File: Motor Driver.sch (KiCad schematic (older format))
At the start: 45 parts, among them CON1 AVR-ISP-6, J1 Conn_01x02, J10 Conn_01x04, J2 Conn_01x02, J3 Conn_01x04, J4 Conn_01x04, J5 Conn_01x04, J6 Conn_02x02_Odd_Even, J7 Conn_01x02, J8 Conn_01x02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

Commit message: Added Isolation
Added an Optoisolator to isolate the input signal
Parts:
- added J11: Conn_01x02, Pin_Headers:Pin_Header_Straight_1x02_Pitch2.54mm, symbol Conn_01x02
- added R14, R15, R16: 200, Resistors_THT:R_Axial_DIN0207_L6.3mm_D2.5mm_P7.62mm_Horizontal, symbol R
- added U2: PC817, Housings_DIP:DIP-4_W7.62mm, symbol PC817
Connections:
- net labels added: INPUT_L
- wire segments 141 -> 152
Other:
- moved on the sheet: J1

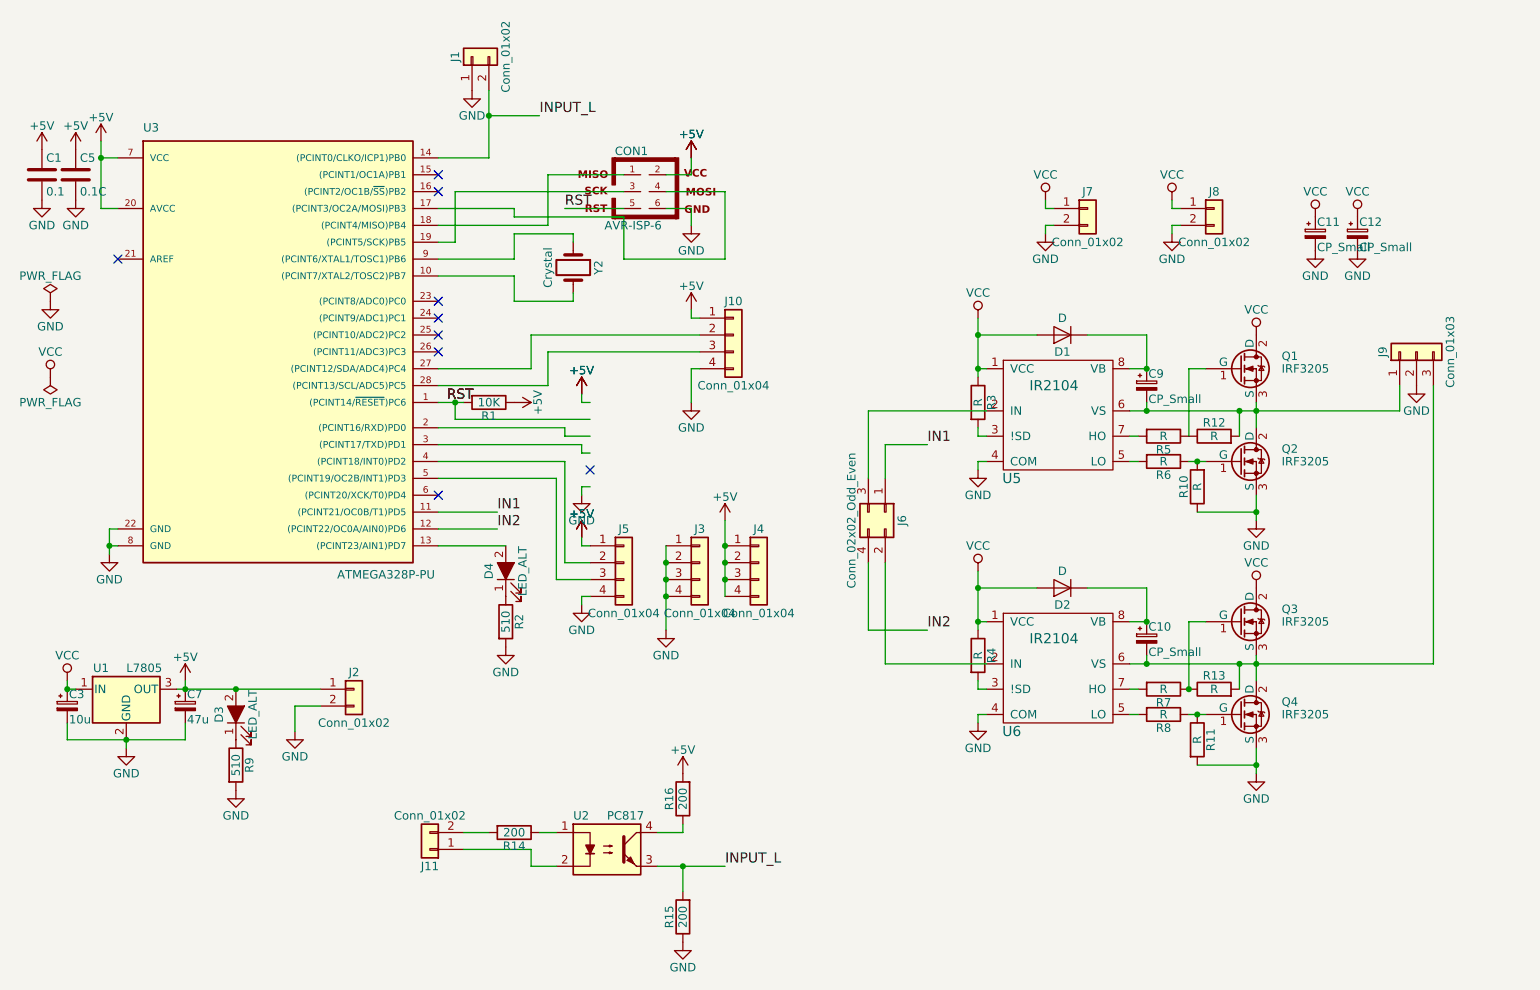
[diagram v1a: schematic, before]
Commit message: Seecond iteration
Modified according to the new motor acquired
Fixed errors in the SCH->Added gate diodes
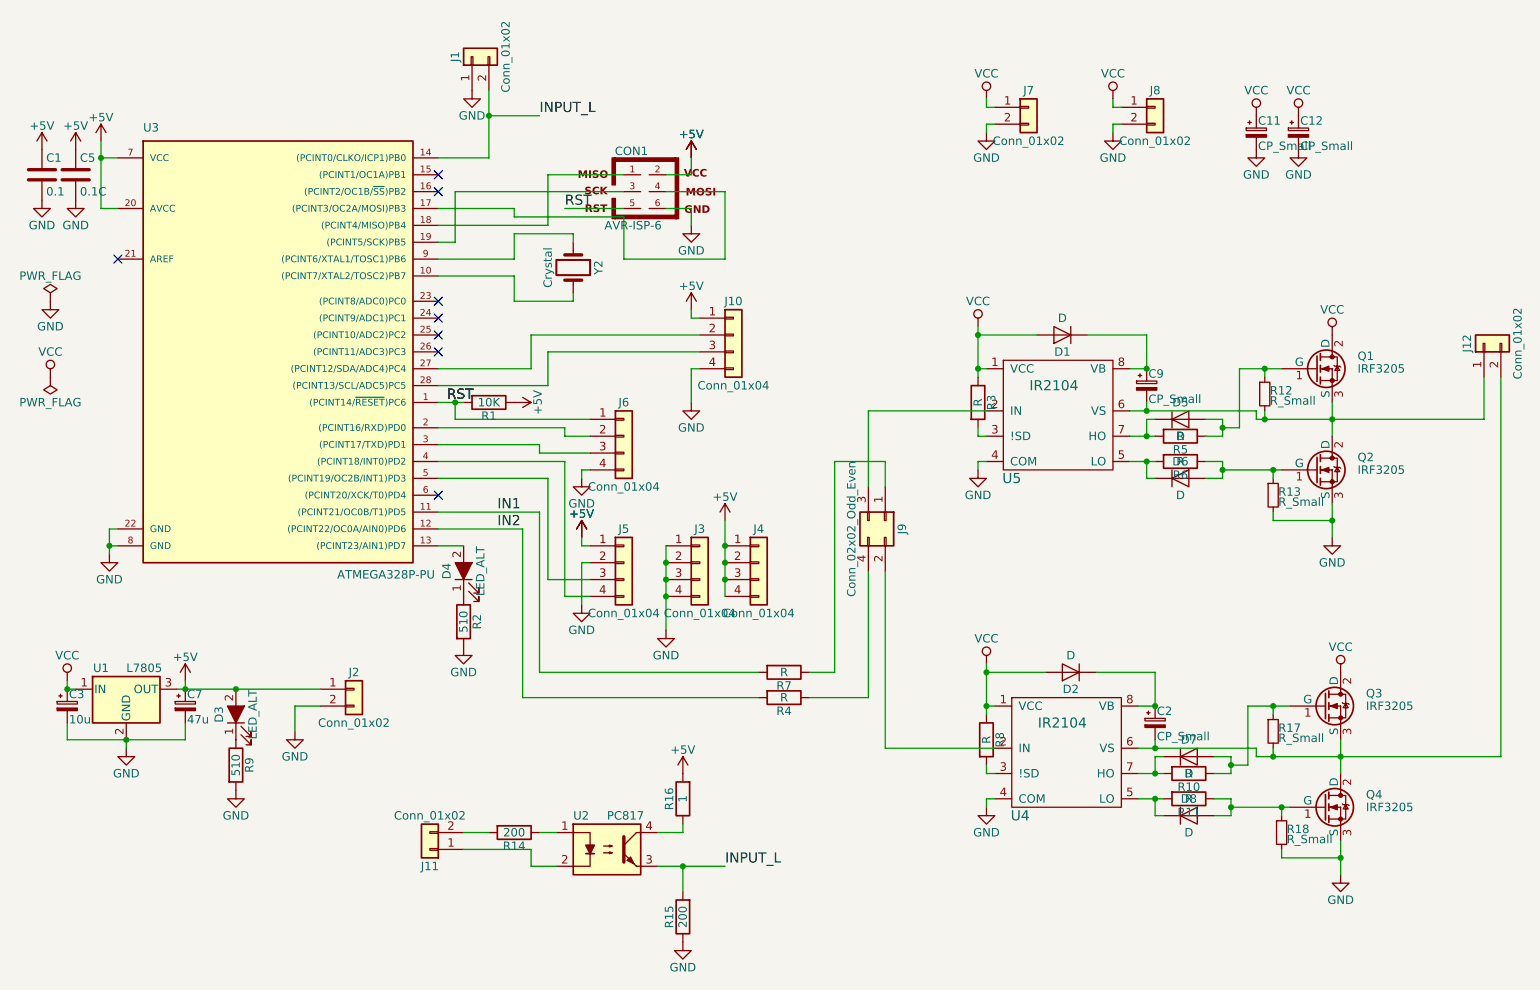
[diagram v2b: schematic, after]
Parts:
- removed C10: CP_Small, Capacitors_THT:CP_Radial_D5.0mm_P2.00mm, symbol CP_Small
- removed J6: Conn_02x02_Odd_Even, Pin_Headers:Pin_Header_Straight_2x02_Pitch2.54mm, symbol Conn_02x02_Odd_Even
- removed J9: Conn_01x03, Connectors_WAGO:WAGO_734_3pin_Straight_RuggedPads, symbol Conn_01x03
- removed R12, R13: R, Resistors_THT:R_Axial_DIN0207_L6.3mm_D2.5mm_P7.62mm_Horizontal, symbol R
- removed U6: IR2104, Housings_DIP:DIP-8_W7.62mm_Socket_LongPads, symbol IR2104
- added C2: CP_Small, Capacitors_THT:CP_Radial_D5.0mm_P2.00mm, symbol CP_Small
- added D5, D6, D7, D8: D, Diodes_THT:D_A-405_P7.62mm_Horizontal, symbol D
- added J12: Conn_01x02, Connectors_WAGO:WAGO_734_2pin_Straight_RuggedPads, symbol Conn_01x02
- added J6: Conn_01x04, Pin_Headers:Pin_Header_Straight_1x04_Pitch2.54mm, symbol Conn_01x04
- added J9: Conn_02x02_Odd_Even, Pin_Headers:Pin_Header_Straight_2x02_Pitch2.54mm, symbol Conn_02x02_Odd_Even
- added R12, R13, R17, R18: R_Small, Resistors_THT:R_Axial_DIN0207_L6.3mm_D2.5mm_P7.62mm_Horizontal, symbol R_Small
- added U4: IR2104, Housings_DIP:DIP-8_W7.62mm_Socket_LongPads, symbol IR2104
- C7: footprint Capacitors_THT:CP_Radial_D10.0mm_P2.50mm_P5.00mm -> Capacitors_THT:CP_Radial_D6.3mm_P2.50mm
- J5: footprint Pin_Headers:Pin_Header_Straight_1x04_Pitch2.54mm -> Connectors_JST:JST_XH_B04B-XH-A_04x2.50mm_Straight
- R16: value 200 -> 1
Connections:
- wire segments 152 -> 190
- no-connect marks 9 -> 8
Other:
- moved on the sheet: C11, C12, D4, J7, J8, Q1, Q2, R2, R5, R6
